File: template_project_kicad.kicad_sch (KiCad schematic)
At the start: 1 part

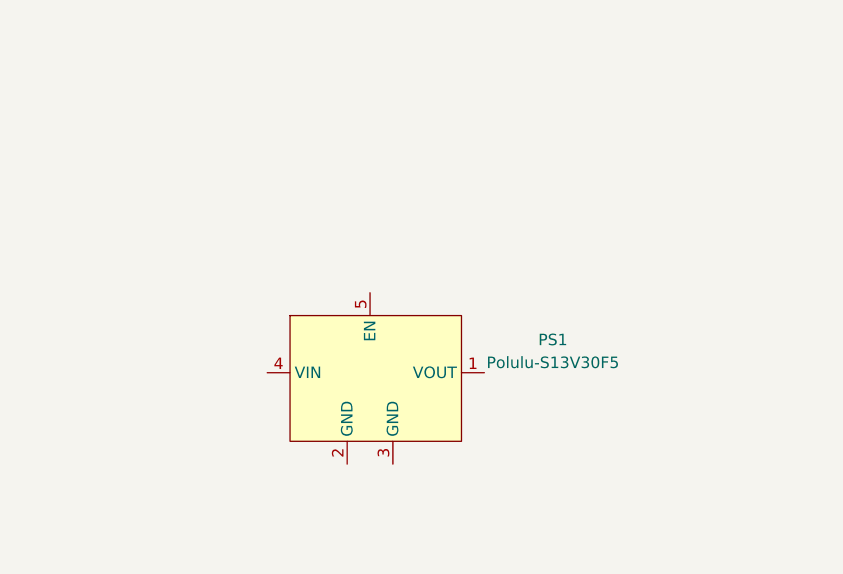
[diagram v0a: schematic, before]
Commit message: Updated paths and replaced voltage regulator with raspberry pi pico in template
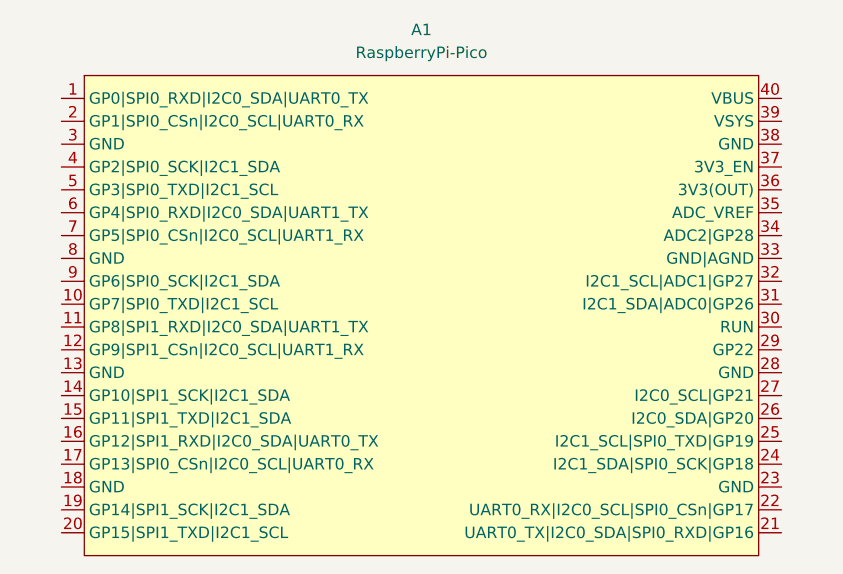
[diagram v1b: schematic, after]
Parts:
- removed PS1: Polulu-S13V30F5, twyleg-voltage-regulators:Polulu-S13V30F5, symbol twyleg-voltage-regulators:Polulu-S13V30F5
- added A1: RaspberryPi-Pico, twyleg-board-connectors:RaspberryPiPico-THT-Dev, symbol twyleg-board-connectors:RaspberryPi-Pico
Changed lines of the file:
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@@
 (kicad_sch (version 20230121) (generator eeschema)
   (paper "A4")
-  (symbol (lib_id "twyleg-voltage-regulators:Polulu-S13V30F5") (at 134.62 72.39 0) (unit 1)
+  (symbol (lib_id "twyleg-board-connectors:RaspberryPi-Pico") (at 139.7 52.07 0) (unit 1)
     (in_bom yes) (on_board yes) (dnp no) (fields_autoplaced)
-    (property "Reference" "PS1" (at 154.94 81.4421 0)
+    (property "Reference" "A1" (at 140.335 46.99 0)
       (effects (font (size 1.27 1.27)))
     )
-    (property "Value" "Polulu-S13V30F5" (at 154.94 83.9821 0)
+    (property "Value" "RaspberryPi-Pico" (at 140.335 49.53 0)
       (effects (font (size 1.27 1.27)))
     )
-    (property "Footprint" "twyleg-voltage-regulators:Polulu-S13V30F5" (at 134.62 72.39 0)
+    (property "Footprint" "twyleg-board-connectors:RaspberryPiPico-THT-Dev" (at 139.7 109.22 0)
       (effects (font (size 1.27 1.27)) hide)
     )
-    (property "Datasheet" "" (at 134.62 72.39 0)
+    (property "Datasheet" "" (at 132.08 54.61 0)
       (effects (font (size 1.27 1.27)) hide)
     )
+    (pin "7")
+    (pin "34")
+    (pin "38")
+    (pin "26")
+    (pin "20")
+    (pin "18")
+    (pin "23")
+    (pin "37")
+    (pin "6")
+    (pin "17")
+    (pin "31")
+    (pin "29")
+    (pin "19")
+    (pin "36")
+    (pin "35")
+    (pin "25")
+    (pin "12")
+    (pin "9")
+    (pin "24")
+    (pin "27")
+    (pin "32")
     (pin "3")
+    (pin "16")
+    (pin "1")
+    (pin "28")
+    (pin "39")
+    (pin "11")
     (pin "2")
-    (pin "1")
+    (pin "8")
+    (pin "22")
+    (pin "40")
+    (pin "14")
+    (pin "15")
     (pin "4")
+    (pin "21")
+    (pin "13")
+    (pin "10")
+    (pin "33")
+    (pin "30")
     (pin "5")
     (instances
       (project "template_project_kicad"
         (path "/b464f893-b088-4709-8572-04b2e8773c63"
-          (reference "PS1") (unit 1)
+          (reference "A1") (unit 1)
         )
       )

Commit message: Assigned GND net to copper zones
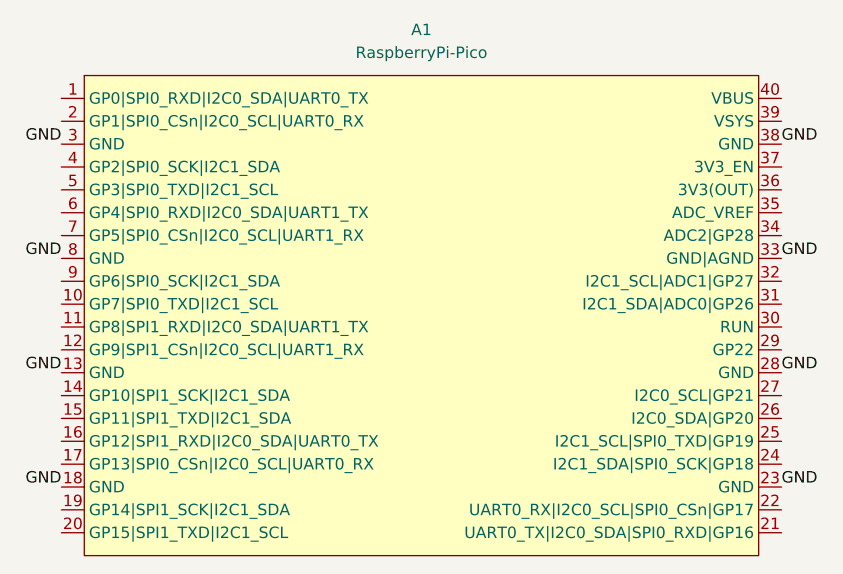
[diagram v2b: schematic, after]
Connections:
- net GND: now reaches A1.13 (GND)
- net GND: now also A1.18 (GND), A1.23 (GND), A1.28 (GND), A1.3 (GND), A1.33 (GND|AGND), A1.38 (GND), A1.8 (GND)
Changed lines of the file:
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@@
 (kicad_sch (version 20230121) (generator eeschema)
   (paper "A4")
+  (label "GND" (at 180.34 59.69 0) (fields_autoplaced)
+    (effects (font (size 1.27 1.27)) (justify left bottom))
+  )
+  (label "GND" (at 100.33 72.39 180) (fields_autoplaced)
+    (effects (font (size 1.27 1.27)) (justify right bottom))
+  )
+  (label "GND" (at 180.34 72.39 0) (fields_autoplaced)
+    (effects (font (size 1.27 1.27)) (justify left bottom))
+  )
+  (label "GND" (at 100.33 59.69 180) (fields_autoplaced)
+    (effects (font (size 1.27 1.27)) (justify right bottom))
+  )
+  (label "GND" (at 180.34 97.79 0) (fields_autoplaced)
+    (effects (font (size 1.27 1.27)) (justify left bottom))
+  )
+  (label "GND" (at 100.33 97.79 180) (fields_autoplaced)
+    (effects (font (size 1.27 1.27)) (justify right bottom))
+  )
+  (label "GND" (at 100.33 85.09 180) (fields_autoplaced)
+    (effects (font (size 1.27 1.27)) (justify right bottom))
+  )
+  (label "GND" (at 180.34 85.09 0) (fields_autoplaced)
+    (effects (font (size 1.27 1.27)) (justify left bottom))
+  )
   (symbol (lib_id "twyleg-board-connectors:RaspberryPi-Pico") (at 139.7 52.07 0) (unit 1)
     (in_bom yes) (on_board yes) (dnp no) (fields_autoplaced)
